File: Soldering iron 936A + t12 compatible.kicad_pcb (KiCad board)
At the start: 2 copper layers, 97 x 67 mm, 120 parts, among them J1 DC INPUT, J10 Conn_01x01_Socket, J11 Conn_01x01_Socket, J2 USB TO SERIAL, J3 AC input, J4 output_connector, J5 mosfet_driver_future_backup, J6 OLED, J7 USB C BREAKOUT BOARD, J8 Conn_01x01_Socket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

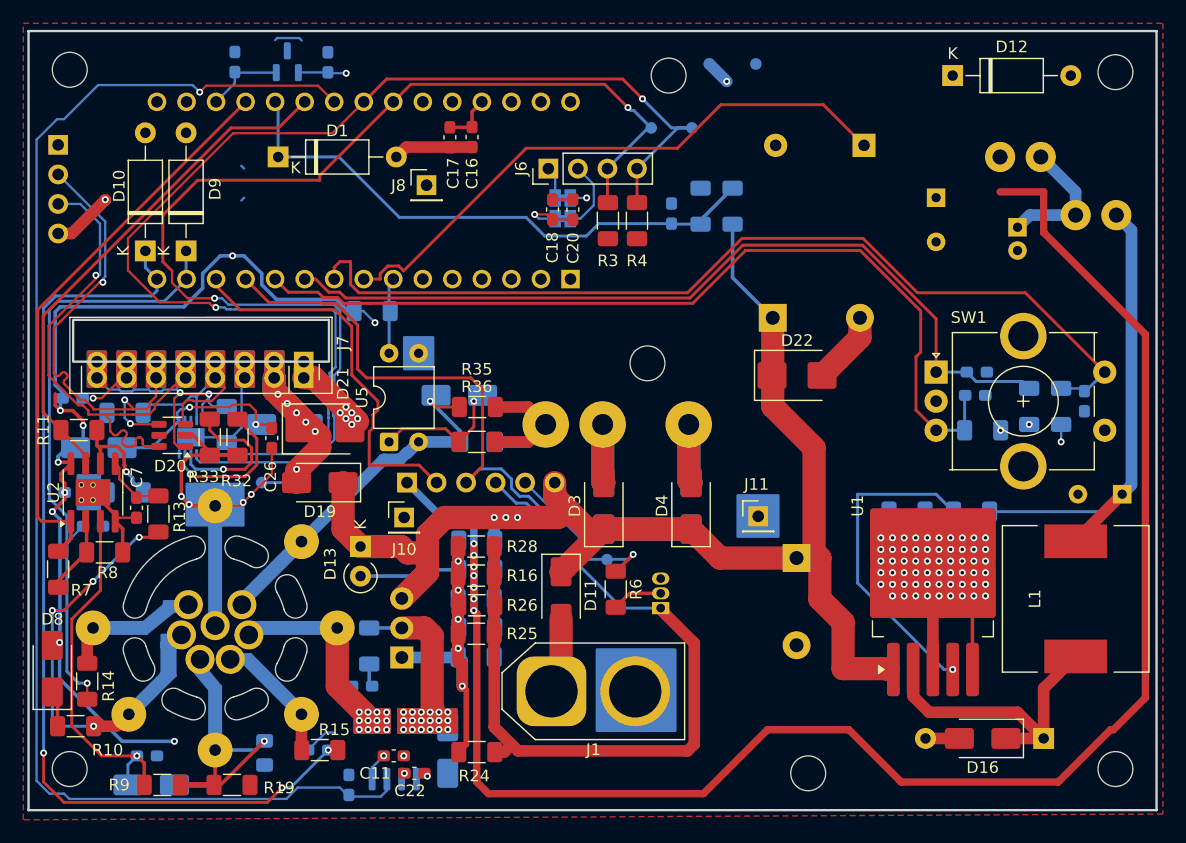
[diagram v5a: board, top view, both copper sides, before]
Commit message: final schematic and layout done need to review though , removed uneccesary features
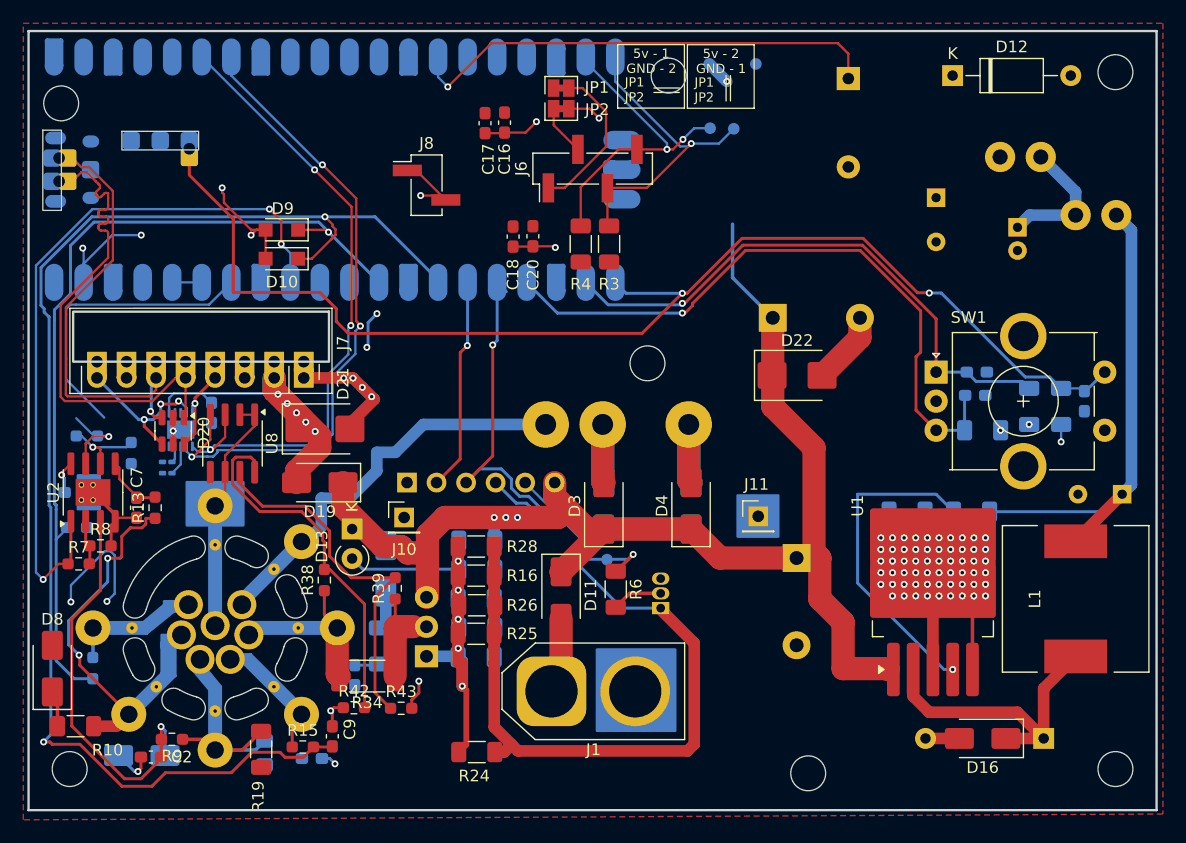
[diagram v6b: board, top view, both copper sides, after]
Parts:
- removed A1: Arduino_Nano_v2.x, Module:Arduino_Nano
- removed C10, C23, C25, C27, C28: 100nf, Capacitor_SMD:C_0603_1608Metric_Pad1.08x0.95mm_HandSolder
- removed C22: 1nf, Capacitor_SMD:C_0603_1608Metric_Pad1.08x0.95mm_HandSolder
- removed D1: 5V, Diode_THT:D_A-405_P10.16mm_Horizontal
- removed D17, D18, D7: SS310, Diode_SMD:D_SMA
- removed F1: Fuse, Fuse:Fuse_1206_3216Metric_Pad1.42x1.75mm_HandSolder
- removed J2: USB TO SERIAL, Connector_PinHeader_2.54mm:PinHeader_1x04_P2.54mm_Vertical
- removed R1: 10k, Resistor_SMD:R_1206_3216Metric_Pad1.30x1.75mm_HandSolder
- removed R2: 100k, Resistor_SMD:R_1206_3216Metric_Pad1.30x1.75mm_HandSolder
- removed R35: 1M, Resistor_SMD:R_1206_3216Metric_Pad1.30x1.75mm_HandSolder
- removed R36: 50K, Resistor_SMD:R_1206_3216Metric_Pad1.30x1.75mm_HandSolder
- removed R37: 10K, Resistor_SMD:R_1206_3216Metric_Pad1.30x1.75mm_HandSolder
- removed U3: ACS712xLCTR-05B, Package_SO:SOIC-8_3.9x4.9mm_P1.27mm
- removed U5: PC817, Package_DIP:DIP-4_W7.62mm
- removed U6: REF3040, Package_TO_SOT_SMD:SOT-23
- removed VBUS1: TestPoint, TestPoint:TestPoint_Pad_D1.0mm
- added A2: RaspberryPi_Pico, Module:RaspberryPi_Pico_SMD, B.Cu at (197.3, 78.1)
- added R39: 10k, Resistor_SMD:R_0603_1608Metric_Pad0.98x0.95mm_HandSolder, F.Cu at (202.5, 114.1)
- added R42: 10k, Resistor_SMD:R_0603_1608Metric_Pad0.98x0.95mm_HandSolder, F.Cu at (198.9, 124.4)
- added R43: 10k, Resistor_SMD:R_0603_1608Metric_Pad0.98x0.95mm_HandSolder, F.Cu at (203.0, 124.4)
- added U8: INA219AxD, Package_SO:SOIC-8_3.9x4.9mm_P1.27mm, F.Cu at (188.5, 101.6)
- C11, C26: moved to B.Cu
- C2, C9, JP1, JP2: moved to F.Cu
- D10, D9: value 5V -> 3.3; footprint Diode_THT:D_A-405_P10.16mm_Horizontal -> Diode_SMD:Nexperia_CFP3_SOD-123W
- D12: value 5V -> 3.3V
- J6: footprint Connector_PinHeader_2.54mm:PinHeader_1x04_P2.54mm_Vertical -> Connector_PinHeader_2.54mm:PinHeader_1x04_P2.54mm_Vertical_SMD_Pin1Left
- J8: value Conn_01x01_Socket -> TOP LEFT; footprint Connector_PinHeader_2.54mm:PinHeader_1x01_P2.54mm_Vertical -> Connector_PinHeader_2.54mm:PinHeader_1x02_P2.54mm_Vertical_SMD_Pin1Left
- R11: footprint Resistor_SMD:R_1206_3216Metric_Pad1.30x1.75mm_HandSolder -> Resistor_SMD:R_0603_1608Metric_Pad0.98x0.95mm_HandSolder; moved to B.Cu
- R12, R13, R7, R8, R9: footprint Resistor_SMD:R_1206_3216Metric_Pad1.30x1.75mm_HandSolder -> Resistor_SMD:R_0603_1608Metric_Pad0.98x0.95mm_HandSolder
- R14: value 4.7k -> 10k; footprint Resistor_SMD:R_1206_3216Metric_Pad1.30x1.75mm_HandSolder -> Resistor_SMD:R_0603_1608Metric_Pad0.98x0.95mm_HandSolder; moved to B.Cu
- R15: value 4.7k -> 10k; footprint Resistor_SMD:R_1206_3216Metric_Pad1.30x1.75mm_HandSolder -> Resistor_SMD:R_0603_1608Metric_Pad0.98x0.95mm_HandSolder
- R17: value 3k -> 1.7k
- R19: value 5M -> 7.5M
- R29, R30, R31: value 5k -> 10k
- R32, R33: footprint Resistor_SMD:R_1206_3216Metric_Pad1.30x1.75mm_HandSolder -> Resistor_SMD:R_0201_0603Metric_Pad0.64x0.40mm_HandSolder; moved to B.Cu
- R34: value 5.1K -> 0.1; footprint Resistor_SMD:R_1206_3216Metric_Pad1.30x1.75mm_HandSolder -> Resistor_SMD:R_2010_5025Metric_Pad1.40x2.65mm_HandSolder; moved to F.Cu
- R38: value 5.1K -> 10k; footprint Resistor_SMD:R_1206_3216Metric_Pad1.30x1.75mm_HandSolder -> Resistor_SMD:R_0603_1608Metric_Pad0.98x0.95mm_HandSolder; moved to F.Cu
- moved R34 24.8 mm to (200.1, 121.6), turned to 180 degrees
- moved R38 22.4 mm to (196.4, 113.4), turned to 90 degrees
- moved D15 16.5 mm to (201.7, 112.4), turned to 90 degrees
- moved D10 11.8 mm to (192.7, 85.8), turned to 180 degrees
- moved JP1 9.45 mm to (216.8, 71.1), turned to 0 degrees
- moved JP2 9.45 mm to (216.8, 72.8), turned to 180 degrees
- moved D9 8.43 mm to (192.7, 83.3), turned to 180 degrees
- moved SCL1 7.10 mm to (231.6, 74.6)
- moved C11 7.04 mm to (195.3, 128.7), turned to 0 degrees
- moved R32 6.41 mm to (182.9, 103.2), turned to 180 degrees
- moved BZ1 5.90 mm to (241.5, 70.3), turned to -90 degrees
- moved C26 5.61 mm to (186.7, 99.0)
- moved R4 5.23 mm to (218.4, 84.5)
- moved R33 4.79 mm to (182.9, 104.2), turned to 180 degrees
- moved C20 4.14 mm to (214.3, 83.8)
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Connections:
- net +5V renamed +3.3V
- net /5v_unfiltered renamed /3.3v_unfiltered
- net /temp_readback renamed /temp_readback_1
- net Net-(A1-D11) renamed /switch_Boost_d
- net Net-(A1-D12) renamed /switch_sleep_d
- C26 pad 1: Net-(D17-K) -> /VIN_USBC
- D20 pad 1: /CC2 -> /D-
- D20 pad 3: /CC1 -> /D+
- D20 pad 4: /D+ -> /CC2
- D20 pad 5: unconnected-(D20-IO4-Pad5) -> GND
- D20 pad 6: /D- -> /CC1
- J4 pad 6: Net-(D18-A) -> Earth
- J6 pad 3: /SCL -> /SCL1
- J6 pad 4: /SDA -> /SDA1
- J7 pad 3: GND -> unconnected-(J7-SUB2-Pad3)
- J7 pad 7: GND -> unconnected-(J7-SUB1-Pad7)
- R3 pad 1: /SCL -> /SCL1
- R34 pad 1: GND -> /MOS_OUT
- R34 pad 2: /CC2 -> /P+
- R38 pad 1: GND -> /P+
- R38 pad 2: /CC1 -> Net-(U8-IN+)
- R4 pad 1: /SDA -> /SDA1
- SCL1 pad 1: /SCL -> /SCL1
- SDA1 pad 1: /SDA -> /SDA1
- U4 pad 1: Net-(D17-K) -> /VIN_USBC
- U4 pad 4: /CC1 -> /CC2
- U4 pad 5: /CC2 -> /CC1
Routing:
- net +3.3V: track 254.1 -> 33.1 mm, vias 23 -> 12
- net /current_sense: track 116.4 -> 0.00 mm, vias 1 -> 0
- net /SDA: track 110.0 -> 55.1 mm, vias 2 -> 3
- net /VIN_ADC: track 48.6 -> 0.00 mm
- net /SCL: track 103.3 -> 56.6 mm, vias 2 -> 3
- net Net-(U8-IN+): track 0.00 -> 31.9 mm
- net Net-(U8-IN-): track 0.00 -> 31.6 mm
- net /switch_sleep_d: track 82.8 -> 114.0 mm, vias 3 -> 2
- net /SDA1: track 0.00 -> 27.4 mm, vias 0 -> 2
- net /SCL1: track 0.00 -> 27.4 mm, vias 0 -> 1
- net /ENCODER S: track 81.2 -> 106.1 mm, vias 0 -> 2
- net Net-(D18-A): track 24.5 -> 0.00 mm, vias 1 -> 0
- net /ENCODER A: track 72.6 -> 48.9 mm, vias 0 -> 1
- net /switch_Boost_d: track 52.7 -> 73.7 mm
- net /ENCODER B: track 77.0 -> 56.1 mm, vias 0 -> 1
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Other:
- outline, holes or cut-outs redrawn
